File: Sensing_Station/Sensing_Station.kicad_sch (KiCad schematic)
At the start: 23 parts, among them J1 Conn_01x06_Pin, Q1 NMOS, SW1 SW_Reed, U1 LM35CAZ/NOPB, U3 LM358

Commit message: detalles pequeños
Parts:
- R3: value 1k -> 10k
- R4: value R -> 20k
- R8: value 1k -> 220
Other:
- note added: "Buscar uno de 10k-100k"
- note added: "Gain = 5 No inversor"
- note added: "Justify that in San Sebastian we wont go to 0 degrees"
- note added: "Light Station"
- note added: "Range 0.67k - 670k"
- note removed: "Decide on Vth. LTSpice?"
- note removed: "Footprint: SOIC-8 Sockets??"
- note removed: "Light and Sound Station"
- moved on the sheet: C1, C2, D1, D3, D4, MK2, Q1, R10, R11, R13, R4, R5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

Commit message: muchos cambios
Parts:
- removed C2: 2.2uF, symbol Device:C
- removed D3: LED, symbol Device:LED
- removed D4: 1N4148W, Diode_SMD:D_SOD-123, symbol Diode:1N4148W
- removed MK2: AOM-4544P-R, AOM-4544P-R:MIC_AOM-4544P-R, symbol AOM-4544P-R:AOM-4544P-R
- removed R13: 30k, symbol Device:R
- removed RV3: R_Potentiometer, symbol Device:R_Potentiometer
- removed unit 1 of U3
- added D2: LED, symbol Device:LED
- added MK1: AOM-4544P-R, AOM-4544P-R:MIC_AOM-4544P-R, symbol AOM-4544P-R:AOM-4544P-R
- added Q2: NPN, symbol Simulation_SPICE:NPN
- added R6: 10k, symbol Device:R
- added R8: 50k, symbol Device:R
- added U2: NE555P, Package_DIP:DIP-8_W7.62mm, symbol Timer:NE555P
- C1: value 100nF -> 10u
- R10: value 220 -> 2.2k
- R11: value R -> 220
- R9: value 2.2k -> 39k
- renumbered R8 to R7
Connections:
- net +5V: now also R10.1, R6.1, R8.1, U2.4 (~{RST}), U2.8 (VCC); no longer RV1.1
- net DAQ_SOUND: now also R11.1, U2.3 (OUT)
- net GND: now also C1.2, D2.1 (K), MK1.N, Q2.3 (E), U2.1 (GND); no longer R10.2
- net at R9.2: now also MK1.P, Q2.2 (B); no longer C1.1
- net at R11.2: now also D2.2 (A)
- new net: Q2.1 (C), R10.2, U2.2 (TRIG)
- new net: R6.2, RV1.1
- new net: C1.1, R8.2, U2.6 (THRES), U2.7 (DISCH)
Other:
- note added: "Sound Station"
- note removed: "Quizá haya que añadir otra resistendcia"
- moved on the sheet: D1, J1, Q1, R1, R2, R4, R5, R7, RV1, U1, U3B, U3C

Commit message: cosas
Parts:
- removed J1: Conn_01x06_Pin, symbol Connector:Conn_01x06_Pin
- removed Q1: NMOS, symbol Simulation_SPICE:NMOS
- removed Q2: NPN, symbol Simulation_SPICE:NPN
- added C2, C3, C4: 0.1u, symbol Device:C
- added J1, J2, J3: Conn_01x02_Pin, symbol Connector:Conn_01x02_Pin
- added Q1: 2N7000, Package_TO_SOT_THT:TO-92_Inline, symbol Transistor_FET:2N7000
- added Q2: BC550, Package_TO_SOT_THT:TO-92_Inline, symbol Transistor_BJT:BC550
- added RV2: R_Potentiometer, symbol Device:R_Potentiometer
- R4: value 20k -> 10k
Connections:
- net +5V: now also C2.1, C3.1, J1.1 (Pin_1)
- net DAQ_LIGHT: now also J2.2 (Pin_2), Q1.3 (D)
- net DAQ_MAG: now also J2.1 (Pin_1)
- net DAQ_SOUND: now also J3.2 (Pin_2)
- net DAQ_TEMP: now also J3.1 (Pin_1)
- net GND: now also C2.2, C3.2, C4.1, J1.2 (Pin_2), Q1.1 (S), Q2.3 (E)
- net at R10.2, U2.2 (TRIG): now also Q2.1 (C)
- net at R4.2, R5.1: now also Q1.2 (G)
- net at MK1.P: now also Q2.2 (B), RV2.2; no longer R9.2
- net at U2.5 (CONT): now also C4.2
- new net: R9.2, RV2.1
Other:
- note added: "100k rated"
- note added: "Between pins 8 and 1"
- note added: "Gain = 5 Sensibility = 10mV/C New Sensibility = 10 mV/C * 5 = 50 mV/C"
- note added: "LED ON -> DAQ = 5V LED OFF -> DAQ = 0V"
- note added: "SW closed -> DAQ = 5V SW open -> DAQ = 0V"
- moved on the sheet: C1, D2, MK1, R10, R11, R7, R8, R9, U2

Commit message: cosas
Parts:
- C4: value 0.1u -> 0.01u
- R2: value 40k -> 39k
- R8: value 50k -> 51k
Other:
- note added: "Gain = 4.9 Sensibility = 10mV/C New Sensibility = 10 mV/C * 4.9 = 49 mV/C"
- note removed: "Gain = 5 Sensibility = 10mV/C New Sensibility = 10 mV/C * 5 = 50 mV/C"
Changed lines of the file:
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@@
 		)
 	)
-	(text "Gain = 5\nSensibility = 10mV/C\n\nNew Sensibility = 10 mV/C * 5 = 50 mV/C"
+	(text "Gain = 4.9\nSensibility = 10mV/C\n\nNew Sensibility = 10 mV/C * 4.9 = 49 mV/C"
 		(exclude_from_sim no)
 		(at 119.634 37.846 0)
@@
 			)
 		)
-		(property "Value" "50k"
+		(property "Value" "51k"
 			(at 181.61 114.2999 0)
 			(show_name no)
@@
 			)
 		)
-		(property "Value" "0.1u"
+		(property "Value" "0.01u"
 			(at 227.33 109.728 90)
 			(show_name no)
@@
 			)
 		)
-		(property "Value" "40k"
+		(property "Value" "39k"
 			(at 104.648 65.024 90)
 			(show_name no)

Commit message: potenciometro
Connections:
- net +5V: now also RV1.1; no longer R4.1
- net DAQ_LIGHT: now also R6.2; no longer RV1.2
- new net: R4.1, RV1.2
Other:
- note removed: "Buscar uno de 10k-100k"
- note removed: "Justify that in San Sebastian we wont go to 0 degrees"
- moved on the sheet: RV1
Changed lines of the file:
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@@
 		)
 	)
-	(text "Justify that in San Sebastian\nwe wont go to 0 degrees"
-		(exclude_from_sim no)
-		(at 33.274 50.546 0)
-		(effects
-			(font
-				(size 1.27 1.27)
-			)
-			(justify left)
-		)
-	)
 	(text "Light Station\n"
 		(exclude_from_sim no)
@@
 	(text "100k rated\n"
 		(exclude_from_sim no)
-		(at 227.33 41.91 0)
+		(at 181.356 44.704 0)
 		(effects
 			(font
@@
 		)
 	)
-	(text "Buscar uno de 10k-100k"
-		(exclude_from_sim no)
-		(at 228.854 38.608 0)
-		(effects
-			(font
-				(size 1.27 1.27)
-			)
-		)
-	)
 	(junction
 		(at 116.84 46.99)
@@
 	)
 	(junction
-		(at 251.46 127)
+		(at 215.9 48.26)
 		(diameter 0)
 		(color 0 0 0 0)
 	)
 	(junction
-		(at 194.31 133.35)
+		(at 251.46 127)
 		(diameter 0)
 		(color 0 0 0 0)
 	)
 	(junction
-		(at 222.25 48.26)
+		(at 194.31 133.35)
 		(diameter 0)
 		(color 0 0 0 0)
@@
 	)
 	(no_connect
-		(at 215.9 46.99)
+		(at 189.23 44.45)
 	)
 	(no_connect
@@
 	(wire
 		(pts
-			(xy 215.9 38.1) (xy 215.9 39.37)
+			(xy 194.31 54.61) (xy 194.31 57.15)
 		)
 		(stroke
@@
 	(wire
 		(pts
-			(xy 194.31 54.61) (xy 194.31 57.15)
+			(xy 41.91 162.56) (xy 41.91 160.02)
 		)
 		(stroke
@@
 	(wire
 		(pts
-			(xy 41.91 162.56) (xy 41.91 160.02)
+			(xy 251.46 127) (xy 265.43 127)
 		)
 		(stroke
@@
 	(wire
 		(pts
-			(xy 251.46 127) (xy 265.43 127)
+			(xy 215.9 48.26) (xy 215.9 52.07)
 		)
 		(stroke
@@
 	(wire
 		(pts
-			(xy 215.9 48.26) (xy 215.9 52.07)
+			(xy 228.6 93.98) (xy 228.6 99.06)
 		)
 		(stroke
@@
 	(wire
 		(pts
-			(xy 228.6 93.98) (xy 228.6 99.06)
+			(xy 116.84 67.31) (xy 116.84 46.99)
 		)
 		(stroke
@@
 	(wire
 		(pts
-			(xy 116.84 67.31) (xy 116.84 46.99)
+			(xy 215.9 38.1) (xy 215.9 48.26)
 		)
 		(stroke
@@
 	(wire
 		(pts
-			(xy 222.25 48.26) (xy 240.03 48.26)
+			(xy 215.9 48.26) (xy 240.03 48.26)
 		)
 		(stroke
@@
 	(wire
 		(pts
-			(xy 240.03 99.06) (xy 237.49 99.06)
+			(xy 189.23 33.02) (xy 189.23 36.83)
 		)
 		(stroke
@@
 	(wire
 		(pts
-			(xy 58.42 118.11) (xy 73.66 118.11)
+			(xy 194.31 46.99) (xy 194.31 40.64)
 		)
 		(stroke
@@
 	(wire
 		(pts
-			(xy 228.6 99.06) (xy 228.6 105.41)
+			(xy 240.03 99.06) (xy 237.49 99.06)
 		)
 		(stroke
@@
 	(wire
 		(pts
-			(xy 93.98 76.2) (xy 93.98 78.74)
+			(xy 194.31 40.64) (xy 193.04 40.64)
 		)
 		(stroke
@@
 	(wire
 		(pts
-			(xy 217.17 129.54) (xy 217.17 127)
+			(xy 58.42 118.11) (xy 73.66 118.11)
 		)
 		(stroke
@@
 	(wire
 		(pts
-			(xy 240.03 48.26) (xy 248.92 48.26)
+			(xy 228.6 99.06) (xy 228.6 105.41)
 		)
 		(stroke
@@
 	(wire
 		(pts
-			(xy 222.25 105.41) (xy 228.6 105.41)
+			(xy 93.98 76.2) (xy 93.98 78.74)
 		)
 		(stroke
@@
 	(wire
 		(pts
-			(xy 93.98 67.31) (xy 93.98 68.58)
+			(xy 217.17 129.54) (xy 217.17 127)
 		)
 		(stroke
@@
 	(wire
 		(pts
-			(xy 52.07 41.91) (xy 50.8 41.91)
+			(xy 240.03 48.26) (xy 248.92 48.26)
 		)
 		(stroke
@@
 	(wire
 		(pts
-			(xy 194.31 43.18) (xy 194.31 46.99)
+			(xy 222.25 105.41) (xy 228.6 105.41)
 		)
 		(stroke
@@
 	(wire
 		(pts
-			(xy 194.31 119.38) (xy 194.31 133.35)
+			(xy 93.98 67.31) (xy 93.98 68.58)
 		)
 		(stroke
@@
 	(wire
 		(pts
-			(xy 36.83 186.69) (xy 43.18 186.69)
+			(xy 52.07 41.91) (xy 50.8 41.91)
 		)
 		(stroke
@@
 	(wire
 		(pts
-			(xy 194.31 68.58) (xy 194.31 71.12)
+			(xy 194.31 119.38) (xy 194.31 133.35)
 		)
 		(stroke
@@
 	(wire
 		(pts
-			(xy 219.71 43.18) (xy 222.25 43.18)
+			(xy 36.83 186.69) (xy 43.18 186.69)
+		)
+		(stroke
+			(width 0)
+			(type default)
+		)
+	)
+	(wire
+		(pts
+			(xy 194.31 68.58) (xy 194.31 71.12)
 		)
 		(stroke
@@
 	(wire
 		(pts
-			(xy 222.25 43.18) (xy 222.25 48.26)
-		)
-		(stroke
-			(width 0)
-			(type default)
-		)
-	)
-	(wire
-		(pts
 			(xy 36.83 184.15) (xy 43.18 184.15)
 		)
@@
 	(wire
 		(pts
-			(xy 215.9 48.26) (xy 222.25 48.26)
-		)
-		(stroke
-			(width 0)
-			(type default)
-		)
-	)
-	(wire
-		(pts
 			(xy 217.17 113.03) (xy 223.52 113.03)
 		)
@@
 	(symbol
 		(lib_id "power:+5V")
-		(at 194.31 43.18 0)
+		(at 189.23 33.02 0)
 		(unit 1)
 		(body_style 1)
@@
 		(fields_autoplaced yes)
 		(property "Reference" "#PWR023"
-			(at 194.31 46.99 0)
+			(at 189.23 36.83 0)
 			(hide yes)
 			(show_name no)
@@
 		)
 		(property "Value" "+5V"
-			(at 194.31 38.1 0)
+			(at 189.23 27.94 0)
 			(show_name no)
 			(do_not_autoplace no)
@@
 		)
 		(property "Footprint" ""
-			(at 194.31 43.18 0)
+			(at 189.23 33.02 0)
 			(hide yes)
 			(show_name no)
@@
 		)
 		(property "Datasheet" ""
-			(at 194.31 43.18 0)
+			(at 189.23 33.02 0)
 			(hide yes)
 			(show_name no)
@@
 		)
 		(property "Description" "Power symbol creates a global label with name \"+5V\""
-			(at 194.31 43.18 0)
+			(at 189.23 33.02 0)
 			(hide yes)
 			(show_name no)
@@
 	(symbol
 		(lib_id "Device:R_Potentiometer")
-		(at 215.9 43.18 0)
+		(at 189.23 40.64 0)
 		(unit 1)
 		(body_style 1)
@@
 		(dnp no)
 		(property "Reference" "RV1"
-			(at 213.36 41.9099 0)
+			(at 186.69 39.3699 0)
 			(show_name no)
 			(do_not_autoplace no)
@@
 		)
 		(property "Value" "R_Potentiometer"
-			(at 213.106 44.196 0)
+			(at 186.436 41.656 0)
 			(show_name no)
 			(do_not_autoplace no)
@@
 		)
 		(property "Footprint" ""
-			(at 215.9 43.18 0)
+			(at 189.23 40.64 0)
 			(hide yes)
 			(show_name no)
@@
 		)
 		(property "Datasheet" ""
-			(at 215.9 43.18 0)
+			(at 189.23 40.64 0)
 			(hide yes)
 			(show_name no)
@@
 		)
 		(property "Description" "Potentiometer"
-			(at 215.9 43.18 0)
+			(at 189.23 40.64 0)
 			(hide yes)
 			(show_name no)
@@
 		)
 		(property "Sim.Device" "R"
-			(at 215.9 43.18 0)
+			(at 189.23 40.64 0)
 			(hide yes)
 			(show_name no)
@@
 		)
 		(property "Sim.Type" "POT"
-			(at 215.9 43.18 0)
+			(at 189.23 40.64 0)
 			(hide yes)
 			(show_name no)
@@
 		)
 		(property "Sim.Pins" "1=r0 2=wiper 3=r1"
-			(at 215.9 43.18 0)
+			(at 189.23 40.64 0)
 			(hide yes)
 			(show_name no)

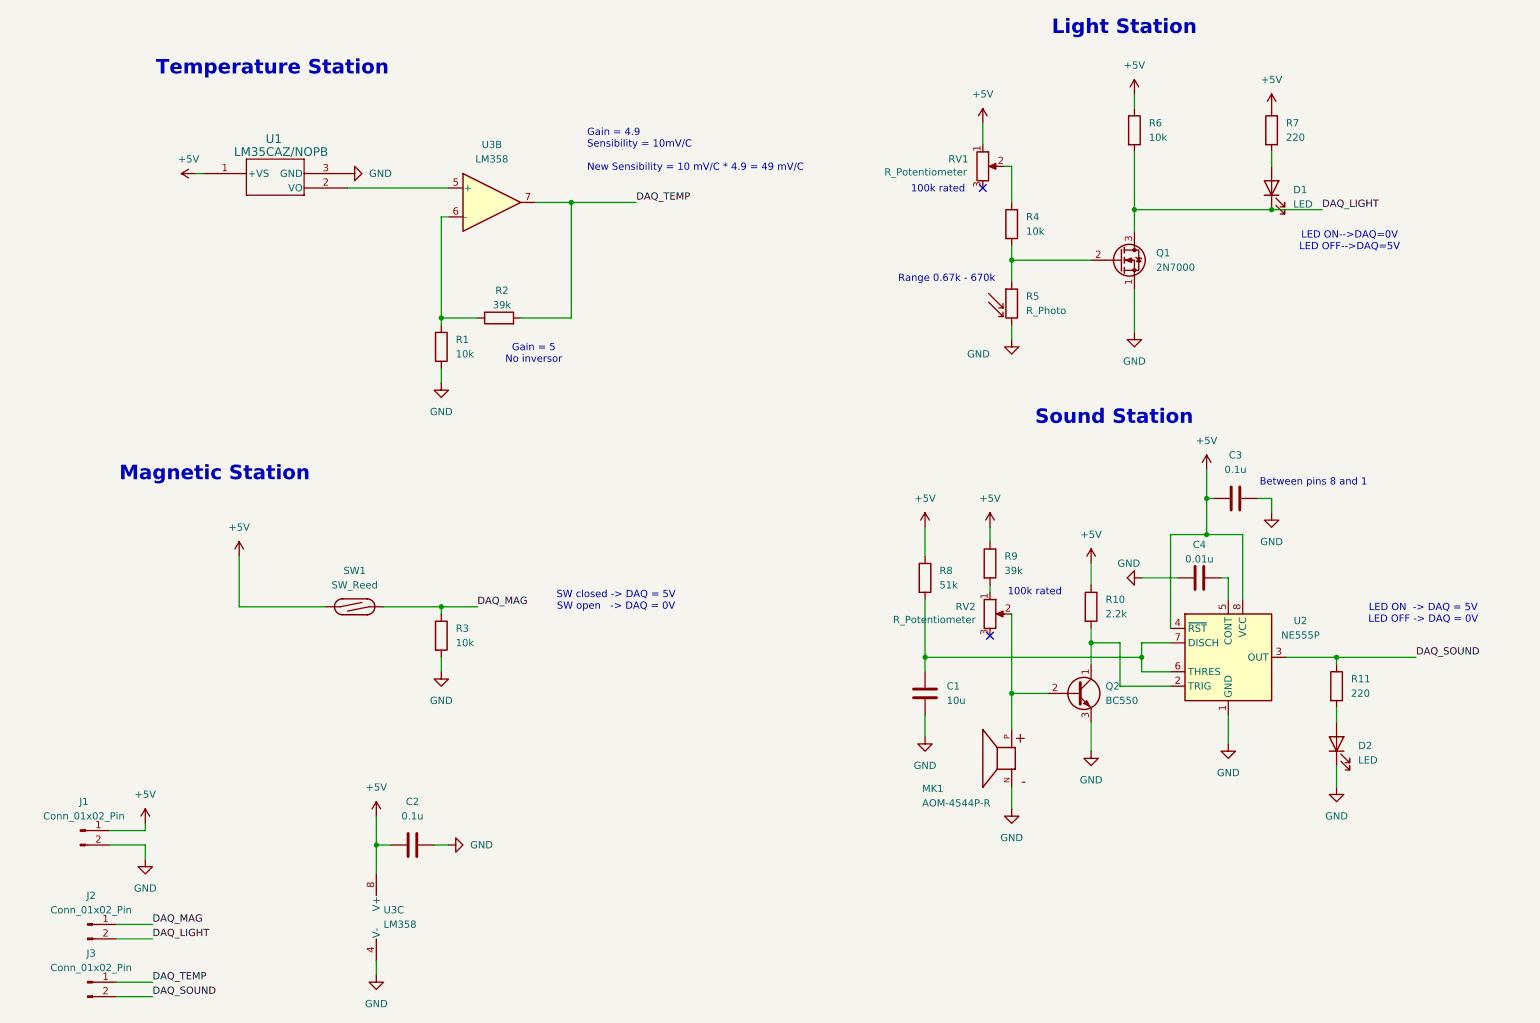
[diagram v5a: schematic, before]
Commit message: resistencia threshold timer
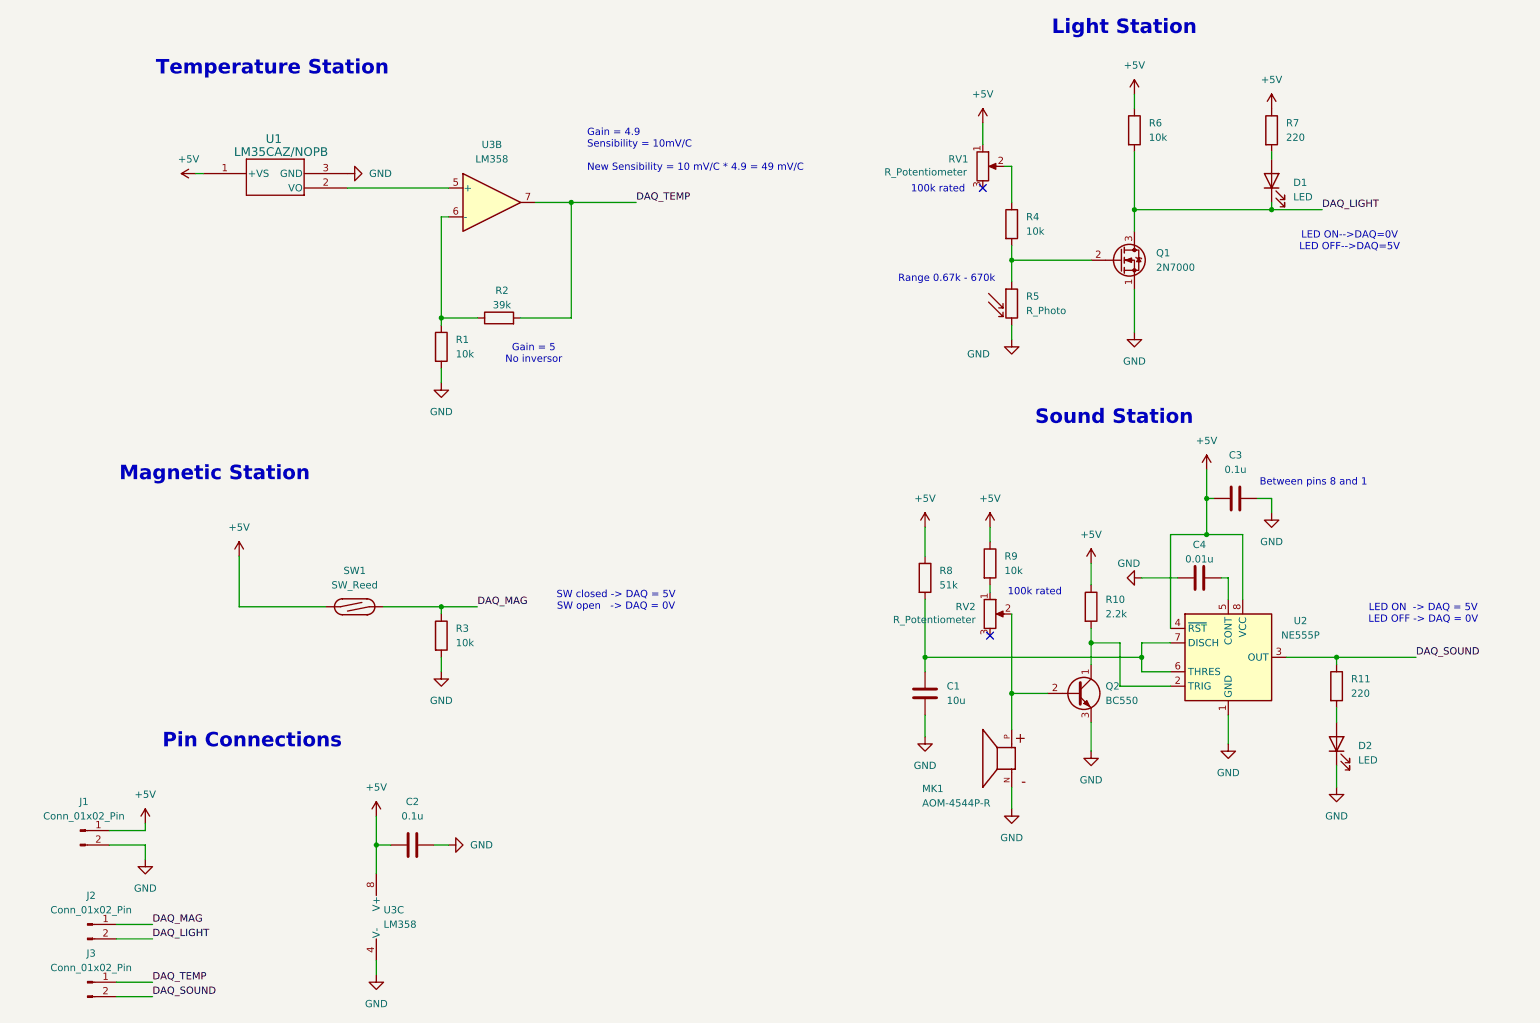
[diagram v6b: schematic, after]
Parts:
- R9: value 39k -> 10k
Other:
- note added: "Pin Connections"
- moved on the sheet: D1
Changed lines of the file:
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@@
 		)
 	)
+	(text "Pin Connections\n"
+		(exclude_from_sim no)
+		(at 60.706 141.732 0)
+		(effects
+			(font
+				(size 2.54 2.54)
+				(thickness 0.508)
+				(bold yes)
+			)
+		)
+	)
 	(junction
 		(at 116.84 46.99)
@@
 	(wire
 		(pts
-			(xy 240.03 38.1) (xy 240.03 40.64)
+			(xy 240.03 38.1) (xy 240.03 39.37)
 		)
 		(stroke
@@
 	(wire
 		(pts
+			(xy 240.03 46.99) (xy 240.03 48.26)
+		)
+		(stroke
+			(width 0)
+			(type default)
+		)
+	)
+	(wire
+		(pts
 			(xy 228.6 105.41) (xy 234.95 105.41)
 		)
@@
 	(symbol
 		(lib_id "Device:LED")
-		(at 240.03 44.45 90)
+		(at 240.03 43.18 90)
 		(unit 1)
 		(body_style 1)
@@
 		(fields_autoplaced yes)
 		(property "Reference" "D1"
-			(at 243.84 44.7674 90)
+			(at 243.84 43.4974 90)
 			(show_name no)
 			(do_not_autoplace no)
@@
 		)
 		(property "Value" "LED"
-			(at 243.84 47.3074 90)
+			(at 243.84 46.0374 90)
 			(show_name no)
 			(do_not_autoplace no)
@@
 		)
 		(property "Footprint" ""
-			(at 240.03 44.45 0)
+			(at 240.03 43.18 0)
 			(hide yes)
 			(show_name no)
@@
 		)
 		(property "Datasheet" ""
-			(at 240.03 44.45 0)
+			(at 240.03 43.18 0)
 			(hide yes)
 			(show_name no)
@@
 		)
 		(property "Description" "Light emitting diode"
-			(at 240.03 44.45 0)
+			(at 240.03 43.18 0)
 			(hide yes)
 			(show_name no)
@@
 		)
 		(property "Sim.Pins" "1=K 2=A"
-			(at 240.03 44.45 0)
+			(at 240.03 43.18 0)
 			(hide yes)
 			(show_name no)
@@
 			)
 		)
-		(property "Value" "39k"
+		(property "Value" "10k"
 			(at 193.04 111.7599 0)
 			(show_name no)
